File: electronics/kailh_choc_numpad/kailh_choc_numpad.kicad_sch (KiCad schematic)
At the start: 134 parts, among them J1 Conn_01x06, U1 PCA9554, U2 PCA9535

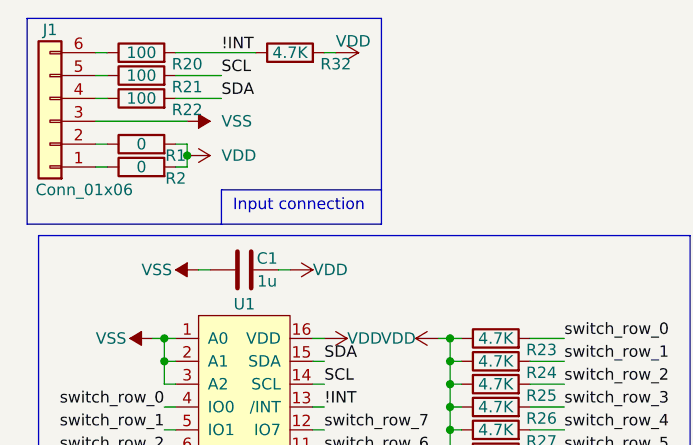
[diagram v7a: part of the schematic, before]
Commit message: further placing and routing
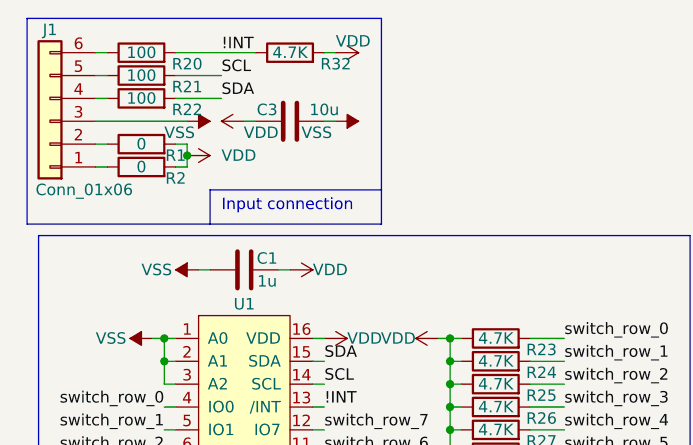
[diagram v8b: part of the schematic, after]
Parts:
- added C3: 10u, SquantorRcl:C_0805, symbol Device:C
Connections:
- net VDD: now also C3.1
- net VSS: now also C3.2
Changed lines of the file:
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@@
     (stroke (width 0) (type default) (color 0 0 0 0))
   )
-  (polyline (pts (xy 53.34 33.02) (xy 35.56 33.02))
+  (polyline (pts (xy 53.34 33.02) (xy 34.29 33.02))
     (stroke (width 0) (type default) (color 0 0 0 0))
   )
@@
     (stroke (width 0) (type default) (color 0 0 0 0))
   )
+  (wire (pts (xy 46.99 25.4) (xy 48.26 25.4))
+    (stroke (width 0) (type default) (color 0 0 0 0))
+  )
   (wire (pts (xy 196.85 97.79) (xy 200.66 97.79))
     (stroke (width 0) (type default) (color 0 0 0 0))
@@
     (stroke (width 0) (type default) (color 0 0 0 0))
   )
-  (polyline (pts (xy 35.56 33.02) (xy 35.56 36.83))
+  (polyline (pts (xy 34.29 33.02) (xy 34.29 36.83))
     (stroke (width 0) (type default) (color 0 0 0 0))
   )
@@
     (stroke (width 0) (type default) (color 0 0 0 0))
   )
+  (wire (pts (xy 38.1 25.4) (xy 39.37 25.4))
+    (stroke (width 0) (type default) (color 0 0 0 0))
+  )
   (wire (pts (xy 45.72 59.69) (xy 46.99 59.69))
     (stroke (width 0) (type default) (color 0 0 0 0))
@@
     (effects (font (size 1.27 1.27)) (justify left bottom))
   )
-  (text "Input connection" (at 36.83 35.56 0)
+  (text "Input connection" (at 35.56 35.56 0)
     (effects (font (size 1.27 1.27)) (justify left bottom))
   )
@@
   )
   (symbol (lib_id "power:VSS") (at 31.75 25.4 270) (unit 1)
-    (in_bom yes) (on_board yes) (fields_autoplaced)
+    (in_bom yes) (on_board yes)
     (property "Reference" "#PWR0103" (id 0) (at 27.94 25.4 0)
       (effects (font (size 1.27 1.27)) hide)
     )
-    (property "Value" "VSS" (id 1) (at 35.56 25.3999 90)
+    (property "Value" "VSS" (id 1) (at 29.21 26.67 90)
       (effects (font (size 1.27 1.27)) (justify left))
     )
@@
     (pin "2")
   )
+  (symbol (lib_id "Device:C") (at 43.18 25.4 90) (unit 1)
+    (in_bom yes) (on_board yes)
+    (property "Reference" "C3" (id 0) (at 40.64 24.13 90))
+    (property "Value" "10u" (id 1) (at 46.99 24.13 90))
+    (property "Footprint" "SquantorRcl:C_0805" (id 2) (at 46.99 24.4348 0)
+      (effects (font (size 1.27 1.27)) hide)
+    )
+    (property "Datasheet" "~" (id 3) (at 43.18 25.4 0)
+      (effects (font (size 1.27 1.27)) hide)
+    )
+    (pin "1")
+    (pin "2")
+  )
   (symbol (lib_id "Device:D") (at 215.9 20.32 180) (unit 1)
     (in_bom yes) (on_board yes)
@@
     (pin "2")
   )
+  (symbol (lib_id "power:VDD") (at 38.1 25.4 90) (unit 1)
+    (in_bom yes) (on_board yes)
+    (property "Reference" "#PWR0120" (id 0) (at 41.91 25.4 0)
+      (effects (font (size 1.27 1.27)) hide)
+    )
+    (property "Value" "VDD" (id 1) (at 41.91 26.67 90)
+      (effects (font (size 1.27 1.27)) (justify left))
+    )
+    (property "Footprint" "" (id 2) (at 38.1 25.4 0)
+      (effects (font (size 1.27 1.27)) hide)
+    )
+    (property "Datasheet" "" (id 3) (at 38.1 25.4 0)
+      (effects (font (size 1.27 1.27)) hide)
+    )
+    (pin "1")
+  )
   (symbol (lib_id "Device:D") (at 215.9 45.72 180) (unit 1)
     (in_bom yes) (on_board yes)
@@
     (pin "2")
   )
+  (symbol (lib_id "power:VSS") (at 48.26 25.4 270) (unit 1)
+    (in_bom yes) (on_board yes)
+    (property "Reference" "#PWR0119" (id 0) (at 44.45 25.4 0)
+      (effects (font (size 1.27 1.27)) hide)
+    )
+    (property "Value" "VSS" (id 1) (at 44.45 26.67 90)
+      (effects (font (size 1.27 1.27)) (justify left))
+    )
+    (property "Footprint" "" (id 2) (at 48.26 25.4 0)
+      (effects (font (size 1.27 1.27)) hide)
+    )
+    (property "Datasheet" "" (id 3) (at 48.26 25.4 0)
+      (effects (font (size 1.27 1.27)) hide)
+    )
+    (pin "1")
+  )
   (symbol (lib_id "SquantorProto:testpad") (at 231.14 132.08 180) (unit 1)
     (in_bom yes) (on_board yes)
@@
       (reference "#PWR0118") (unit 1) (value "VDD") (footprint "")
     )
+    (path "/bc6466b7-adae-4d9c-a869-6b0dfea97c1f"
+      (reference "#PWR0119") (unit 1) (value "VSS") (footprint "")
+    )
+    (path "/af3f290b-498d-491d-94eb-00f8d1a17918"
+      (reference "#PWR0120") (unit 1) (value "VDD") (footprint "")
+    )
     (path "/1ed609c9-f99d-4867-8af9-2413e39d6a8f"
       (reference "C1") (unit 1) (value "1u") (footprint "SquantorRcl:C_0603")
@@
       (reference "C2") (unit 1) (value "1u") (footprint "SquantorRcl:C_0603")
     )
+    (path "/34b32c45-1887-4937-a841-963bfb5c8f2c"
+      (reference "C3") (unit 1) (value "10u") (footprint "SquantorRcl:C_0805")
+    )
     (path "/5fb5dd87-56b4-4a1f-8570-a8900fb63055"
